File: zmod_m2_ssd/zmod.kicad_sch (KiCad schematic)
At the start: 27 parts, among them J1 MDT420M02001, J2 QTH-020-01-X-D-DP-A, U1 SN74LVC1T45DBV, U2 LTC6957xMS-2, X1 ECS-2520MVQ-1000-BN-TR

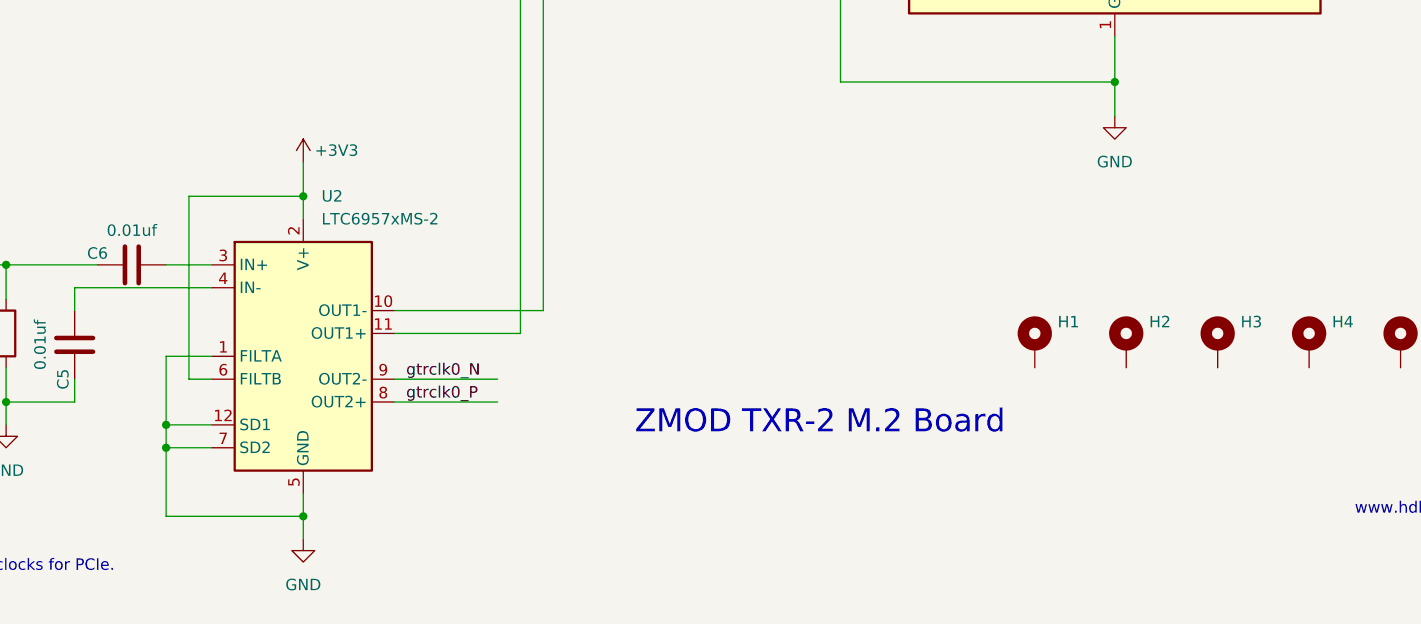
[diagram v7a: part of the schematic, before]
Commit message: Rev B of zmod M.2, changed clock buffer to give full edge rate, reduced M.2 mounting hole from 2.7 to 2.5 mm
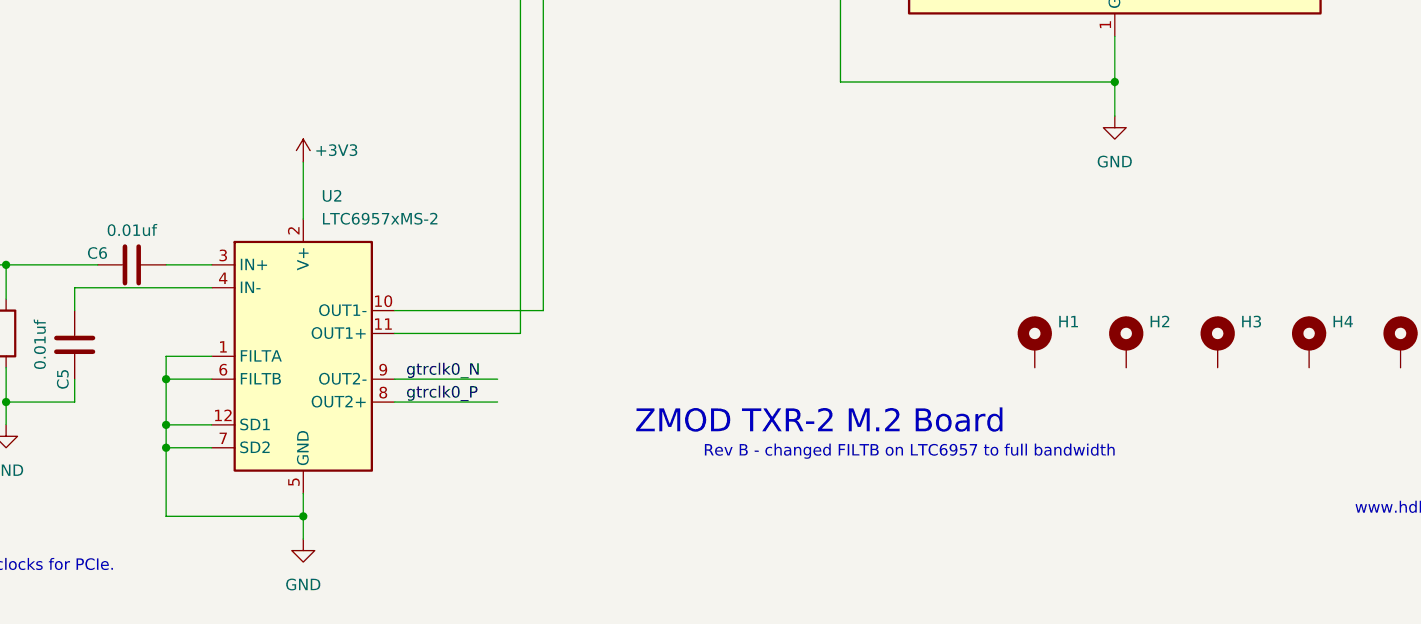
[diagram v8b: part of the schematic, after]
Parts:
- H7: footprint MountingHole:MountingHole_2.7mm_Pad -> MountingHole:MountingHole_2.5mm_Pad
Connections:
- net +3V3: no longer U2.6 (FILTB)
- net GND: now also U2.6 (FILTB)
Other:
- note added: "Rev B - changed FILTB on LTC6957 to full bandwidth"
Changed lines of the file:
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@@
   (junction (at 81.28 123.19) (diameter 0) (color 0 0 0 0)
   )
-  (junction (at 147.32 144.78) (diameter 0) (color 0 0 0 0)
-  )
   (junction (at 114.3 152.4) (diameter 0) (color 0 0 0 0)
   )
@@
   )
   (junction (at 132.08 172.72) (diameter 0) (color 0 0 0 0)
+  )
+  (junction (at 132.08 165.1) (diameter 0) (color 0 0 0 0)
   )
   (junction (at 33.02 186.69) (diameter 0) (color 0 0 0 0)
@@
   (no_connect (at 262.89 99.06))
   (no_connect (at 262.89 106.68))
+  (wire (pts (xy 132.08 165.1) (xy 137.16 165.1))
+    (stroke (width 0) (type default) (color 0 0 0 0))
+  )
   (wire (pts (xy 77.47 92.71) (xy 101.6 92.71))
     (stroke (width 0) (type default) (color 0 0 0 0))
@@
     (stroke (width 0) (type default) (color 0 0 0 0))
   )
-  (wire (pts (xy 137.16 165.1) (xy 134.62 165.1))
-    (stroke (width 0) (type default) (color 0 0 0 0))
-  )
   (wire (pts (xy 132.08 180.34) (xy 147.32 180.34))
     (stroke (width 0) (type default) (color 0 0 0 0))
@@
     (stroke (width 0) (type default) (color 0 0 0 0))
   )
+  (wire (pts (xy 132.08 165.1) (xy 132.08 170.18))
+    (stroke (width 0) (type default) (color 0 0 0 0))
+  )
   (wire (pts (xy 25.4 172.72) (xy 25.4 168.91))
     (stroke (width 0) (type default) (color 0 0 0 0))
@@
     (stroke (width 0) (type default) (color 0 0 0 0))
   )
-  (wire (pts (xy 134.62 144.78) (xy 147.32 144.78))
-    (stroke (width 0) (type default) (color 0 0 0 0))
-  )
   (wire (pts (xy 137.16 162.56) (xy 132.08 162.56))
     (stroke (width 0) (type default) (color 0 0 0 0))
   )
-  (wire (pts (xy 134.62 165.1) (xy 134.62 144.78))
-    (stroke (width 0) (type default) (color 0 0 0 0))
-  )
   (wire (pts (xy 137.16 40.64) (xy 139.7 40.64))
     (stroke (width 0) (type default) (color 0 0 0 0))
@@
     (stroke (width 0) (type default) (color 0 0 0 0))
   )
-  (wire (pts (xy 147.32 140.97) (xy 147.32 144.78))
-    (stroke (width 0) (type default) (color 0 0 0 0))
-  )
   (wire (pts (xy 139.7 46.99) (xy 127 46.99))
     (stroke (width 0) (type default) (color 0 0 0 0))
@@
     (stroke (width 0) (type default) (color 0 0 0 0))
   )
-  (wire (pts (xy 147.32 144.78) (xy 147.32 147.32))
+  (wire (pts (xy 147.32 140.97) (xy 147.32 147.32))
     (stroke (width 0) (type default) (color 0 0 0 0))
   )
@@
     (stroke (width 0) (type default) (color 0 0 0 0))
   )
-  (wire (pts (xy 132.08 162.56) (xy 132.08 170.18))
+  (wire (pts (xy 132.08 162.56) (xy 132.08 165.1))
     (stroke (width 0) (type default) (color 0 0 0 0))
   )
@@
   )
   (text "This is a M-key M.2 connector for an NVMe SSD." (at 186.69 30.48 0)
+    (effects (font (size 1.27 1.27)) (justify left bottom))
+  )
+  (text "Rev B - changed FILTB on LTC6957 to full bandwidth"
+    (at 191.77 173.99 0)
     (effects (font (size 1.27 1.27)) (justify left bottom))
   )
@@
       (effects (font (size 1.27 1.27)) (justify left) hide)
     )
-    (property "Footprint" "MountingHole:MountingHole_2.7mm_Pad" (id 2) (at 279.4 151.13 0)
+    (property "Footprint" "MountingHole:MountingHole_2.5mm_Pad" (id 2) (at 279.4 151.13 0)
       (effects (font (size 1.27 1.27)) hide)
     )
@@
     )
     (path "/5216a05f-00bb-4954-a8d0-d0c5066122b7"
-      (reference "H7") (unit 1) (value "MountingHole_Pad") (footprint "MountingHole:MountingHole_2.7mm_Pad")
+      (reference "H7") (unit 1) (value "MountingHole_Pad") (footprint "MountingHole:MountingHole_2.5mm_Pad")
     )
     (path "/713a8cb6-be5c-413a-968b-156735b7e9f4"
